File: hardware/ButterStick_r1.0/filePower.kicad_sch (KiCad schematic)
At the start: 65 parts, among them J7 Conn_01x02_Male, Q4 Q_PMOS_GSD, Q5 Q_NMOS_GSD, U10 TLV62569DRL, U16 TLV75801PDRV, U17 TLV75801PDRV, U18 TLV6001DCK, U19 LM74700, U6 TLV62569DRL, U7 TLV62569DRL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

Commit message: hw.r1d0: Review complete, gerbers generated
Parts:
- removed Q4: Q_PMOS_GSD, Package_TO_SOT_SMD:SOT-23, symbol Device:Q_PMOS_GSD
- removed Q5: Q_NMOS_GSD, Package_TO_SOT_SMD:SOT-23, symbol Device:Q_NMOS_GSD
- removed U18: TLV6001DCK, Package_TO_SOT_SMD:SOT-353_SC-70-5, symbol Amplifier_Operational:TLV6001DCK
- added C165: 150uF, Capacitor_SMD:CP_Elec_5x4.4, symbol Device:CP1
- added C166: 1uF, Capacitor_SMD:C_0402_1005Metric, symbol Device:C
- added C167: 0.1uF, Capacitor_SMD:C_0402_1005Metric, symbol Device:C
- added Q4: Q_NMOS_GSD, Package_SON:Diodes_PowerDI3333-8, symbol Device:Q_NMOS_GSD
- added R95: 23.7k, Resistor_SMD:R_0402_1005Metric, symbol Device:R
- added U18: TPS2121, gkl_housings_qfn:VQFN-HR, symbol gkl_pmic:TPS2121
- C144: value 0.1uF -> 0.01uF; SN-DK 1276-1002-1-ND -> (none)
- C29, C61, C76, C77, C78: value 0.1uF -> 4.7uF
- C31: value 1uF -> 4.7uF
- C55, C74, C82, C83, C84: value 4.7uF -> 10uF
- C75, C85, C86, C87: value 0.1uF -> 1uF
- R60, R73, R74, R90: value 13.0K -> 180k
- R91: value 53.6K -> 23.7k
- R92, R96: value 53.6K -> 5k
- R97: value 53.6K -> 47k; Tol 1% -> (none)
- U16, U17: PN (none) -> TLV75801PDRVR
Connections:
- net +5V: now also C165.1, U18.1 (OUT), U18.8 (OUT); no longer R96.2, U19.4 (CATHODE)
- net GND: now also C144.2, R96.1, C165.2, C166.2, U18.12 (GND), U18.3 (CP2), U18.6 (PR1), U18.9 (ST)
- net VBUS_USB: now also R91.2, U18.7 (IN1)
- net at J7.1 (Pin_1), U19.3 (EN), U19.6 (ANODE): now also C166.1, C167.1, Q4.3 (D); no longer C143.1, C144.1, R91.2
- net at R91.1, R92.2: now also U18.5 (OV1)
- net at R97.2: now also U18.10 (ILIM); no longer R96.1
- net at U19.5 (GATE): now also Q4.1 (G)
- net at U19.1 (VCAP): now also C167.2; no longer C144.2
- net P_1V2_A renamed P_1V1_A
- net P_1V2_T renamed P_1V1_T
- new net: C143.1, Q4.2 (S), R95.2, U18.2 (IN2), U19.4 (CATHODE)
- new net: R95.1, R96.2, U18.4 (OV2)
- new net: C144.1, U18.11 (SS)
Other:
- note added: "IN2 takes priority over IN1"
- moved on the sheet: C143, C29, C31, C41, C54, C55, C57, C61, C68, C73, C74, C75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

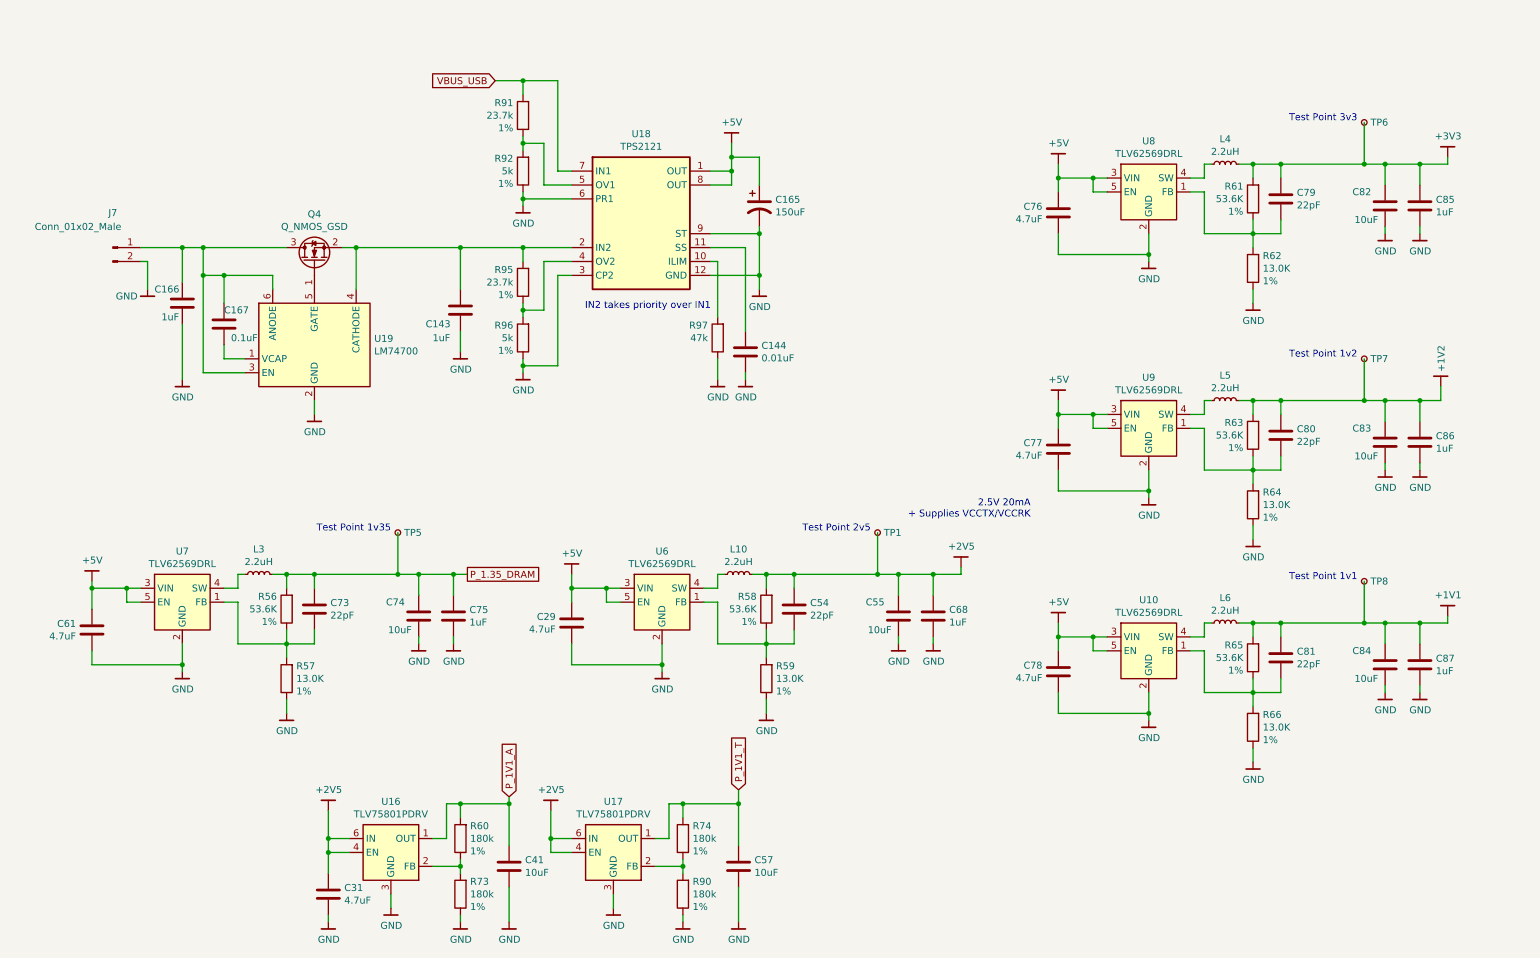
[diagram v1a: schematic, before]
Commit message: hw.r1d0: Update BOM fieids in schematic.
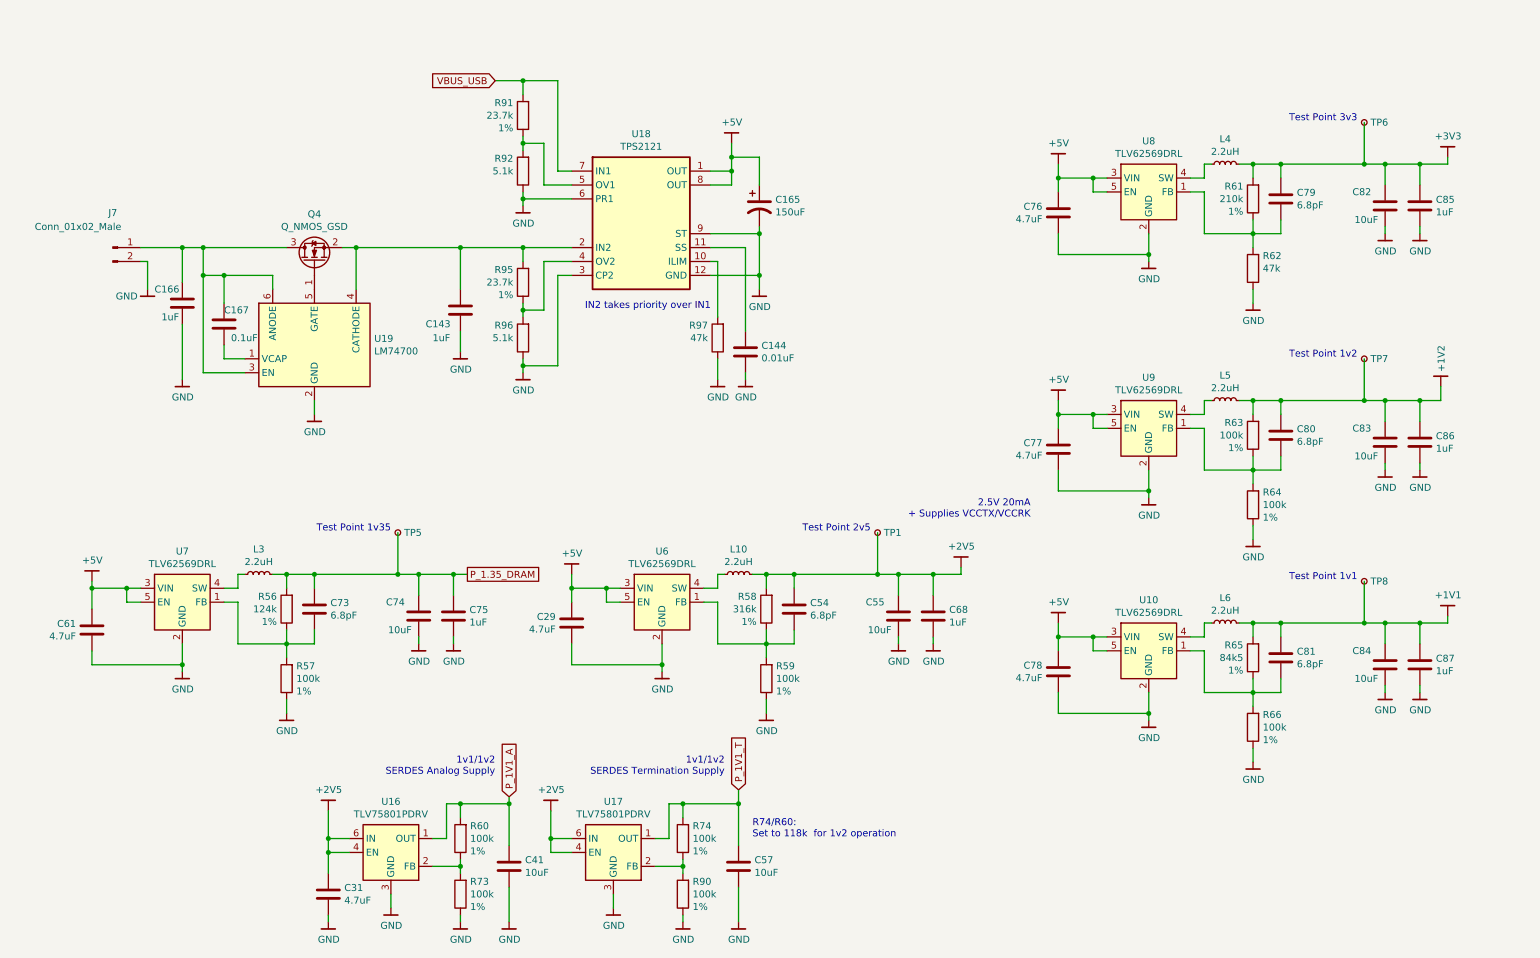
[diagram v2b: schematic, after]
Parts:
- C143, C166: Mfg Samsung Electro-Mechanics -> Yageo; PN CL05B104KP5NNNC -> CC0402KRX5R6BB105; SN-DK 1276-1002-1-ND -> (none)
- C144: Mfg Samsung Electro-Mechanics -> Yageo
- C165: Mfg (none) -> United Chemi-Con
- C167: Mfg Samsung Electro-Mechanics -> Yageo; PN CL05B104KP5NNNC -> CC0402KRX5R6BB104; SN-DK 1276-1002-1-ND -> (none); Tol (none) -> 10V / X5R
- C29, C61, C76, C77, C78: Mfg Samsung Electro-Mechanics -> Yageo; PN CL05B104KP5NNNC -> CC0402MRX5R6BB475
- C31: Mfg Samsung Electro-Mechanics -> Yageo; PN CL05A105KP5NNNC -> CC0402MRX5R6BB475; SN-DK 445-13185-1-ND -> (none)
- C41, C57: Mfg (none) -> Yageo; PN CL10A106MP8NNNC -> CC0603KRX5R5BB106; SN-DK 445-7486-1-ND -> (none)
- C54, C73, C79, C80, C81: value 22pF -> 6.8pF; Mfg Samsung Electro-Mechanics -> Yageo; PN CL05B104KP5NNNC -> CC0402CRNPO9BN6R8
- C55, C74, C82, C83, C84: Mfg Samsung Electro-Mechanics -> Yageo; PN CL10A475KP8NNNC -> CC0603KRX5R5BB106
- C68: Mfg Samsung Electro-Mechanics -> Yageo; PN CL05A105KP5NNNC -> CC0402KRX5R6BB105; SN-DK 445-13185-1-ND -> (none)
- C75, C85, C86, C87: Mfg Samsung Electro-Mechanics -> Yageo; PN CL05B104KP5NNNC -> CC0402KRX5R6BB105
- J7, TP1, TP5, TP6, TP7, TP8: PN (none) -> DNP
- L10, L3, L4, L5, L6: Mfg (none) -> Sunltech Tech; PN (none) -> SLM20122R2MIT
- Q4: Mfg (none) -> Diodes Incorporated
- R56: value 53.6K -> 124k; Mfg Stackpole Electronics Inc -> Yageo; PN (none) -> RC0402FR-07124KL
- R57, R59, R64, R66: value 13.0K -> 100k; Mfg Stackpole Electronics Inc -> Yageo; PN (none) -> RC0402FR-07100KL
- R58: value 53.6K -> 316k; Mfg Stackpole Electronics Inc -> Yageo; PN (none) -> RC0402FR-07316KL
- R60, R73, R74, R90: value 180k -> 100k; Mfg Stackpole Electronics Inc -> Yageo; PN (none) -> RC0402FR-07100KL
- R61: value 53.6K -> 210k; Mfg Stackpole Electronics Inc -> Yageo; PN (none) -> RC0402FR-07210KL
- R62: value 13.0K -> 47k; Mfg Stackpole Electronics Inc -> Yageo; PN (none) -> RC0402FR-074KL; Tol 1% -> (none)
- R63: value 53.6K -> 100k; Mfg Stackpole Electronics Inc -> Yageo; PN (none) -> RC0402FR-07100KL
- R65: value 53.6K -> 84k5; Mfg Stackpole Electronics Inc -> Yageo; PN (none) -> RC0402FR-0784K5L
- R91, R95: Mfg Stackpole Electronics Inc -> Yageo; PN (none) -> RC0402FR-0723K7L
- R92, R96: value 5k -> 5.1k; Mfg Stackpole Electronics Inc -> Yageo; PN (none) -> RC0402FR-075K1L; Tol 1% -> (none)
- R97: Mfg Stackpole Electronics Inc -> Yageo; PN (none) -> RC0402FR-074KL
- U10, U6, U7, U8, U9: Mfg (none) -> Texas Instruments; PN (none) -> TLV62569DRLR
- U16, U17: Mfg (none) -> Texas Instruments
- U18: Mfg (none) -> Texas Instruments; PN (none) -> TPS2121RUXR
- U19: Mfg (none) -> Texas Instruments; PN (none) -> LM74700QDBVRQ1
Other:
- note added: "1v1/1v2 SERDES Analog Supply"
- note added: "1v1/1v2 SERDES Termination Supply"
- note added: "R74/R60: Set to 118k for 1v2 operation"

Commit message: hw.r1d0: Fix RGMII straps
This commit correctly sets the stop resistos on the RGMII lines to 1K5
instead of DNP.
Also regenerate and add a schematic in PDF format.

Fixes #6
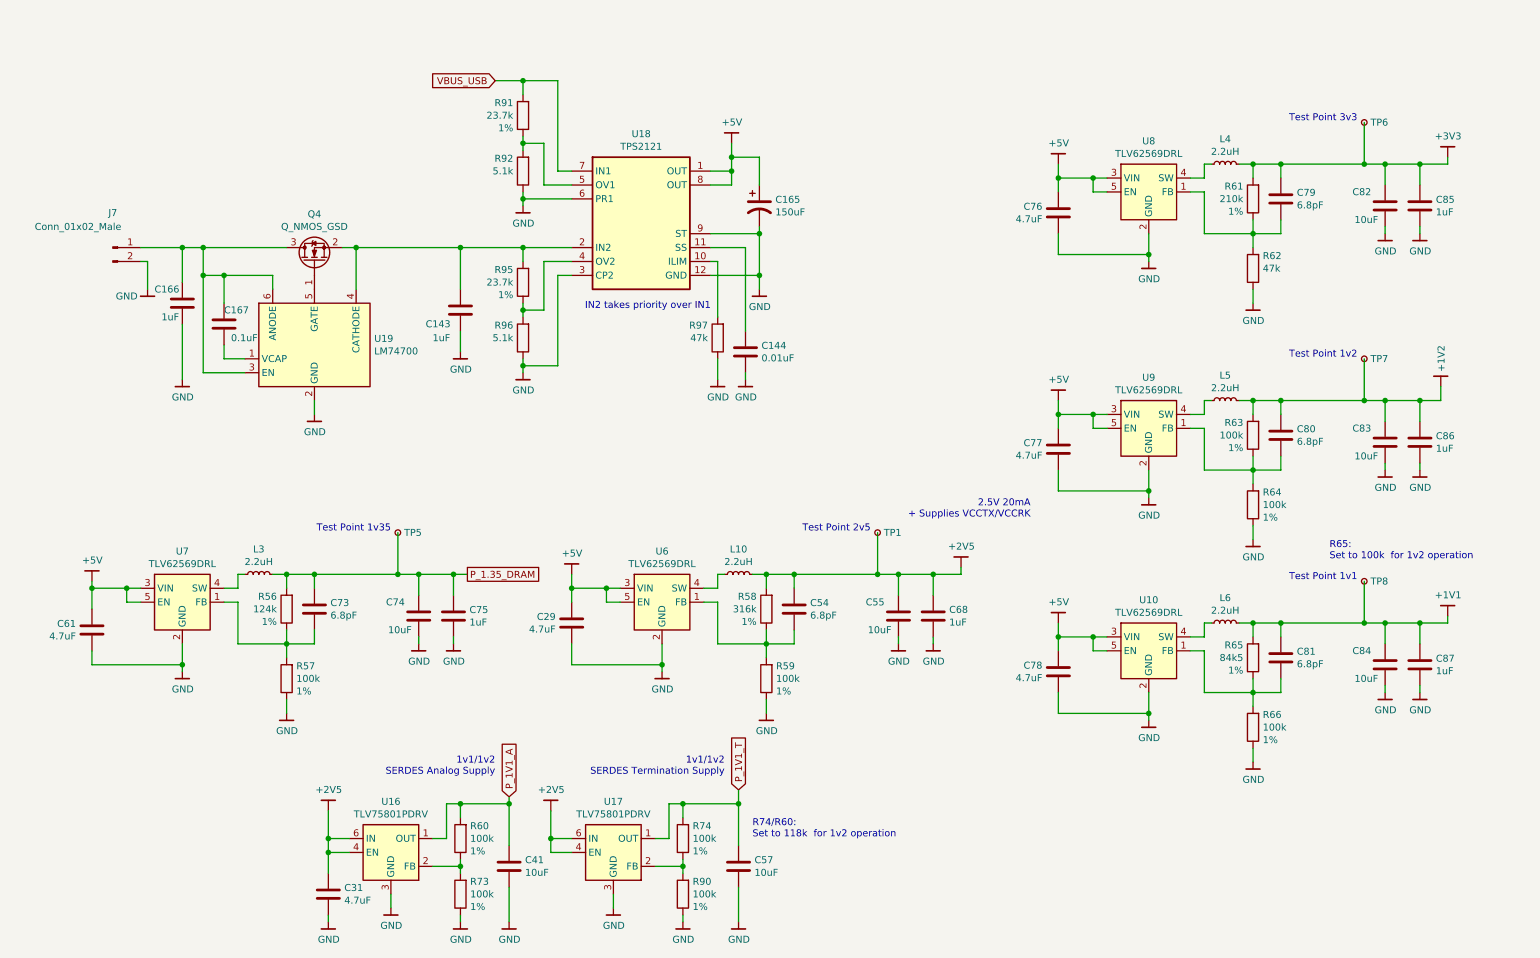
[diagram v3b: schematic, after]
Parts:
- C144: PN CL05B104KP5NNNC -> CC0402KRX7R8BB103
- C29, C31, C61, C76, C77, C78: PN CC0402MRX5R6BB475 -> CC0402KRX5R6BB475
- R62, R97: PN RC0402FR-074KL -> RC0402FR-0747KL
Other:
- note added: "R65: Set to 100k for 1v2 operation"

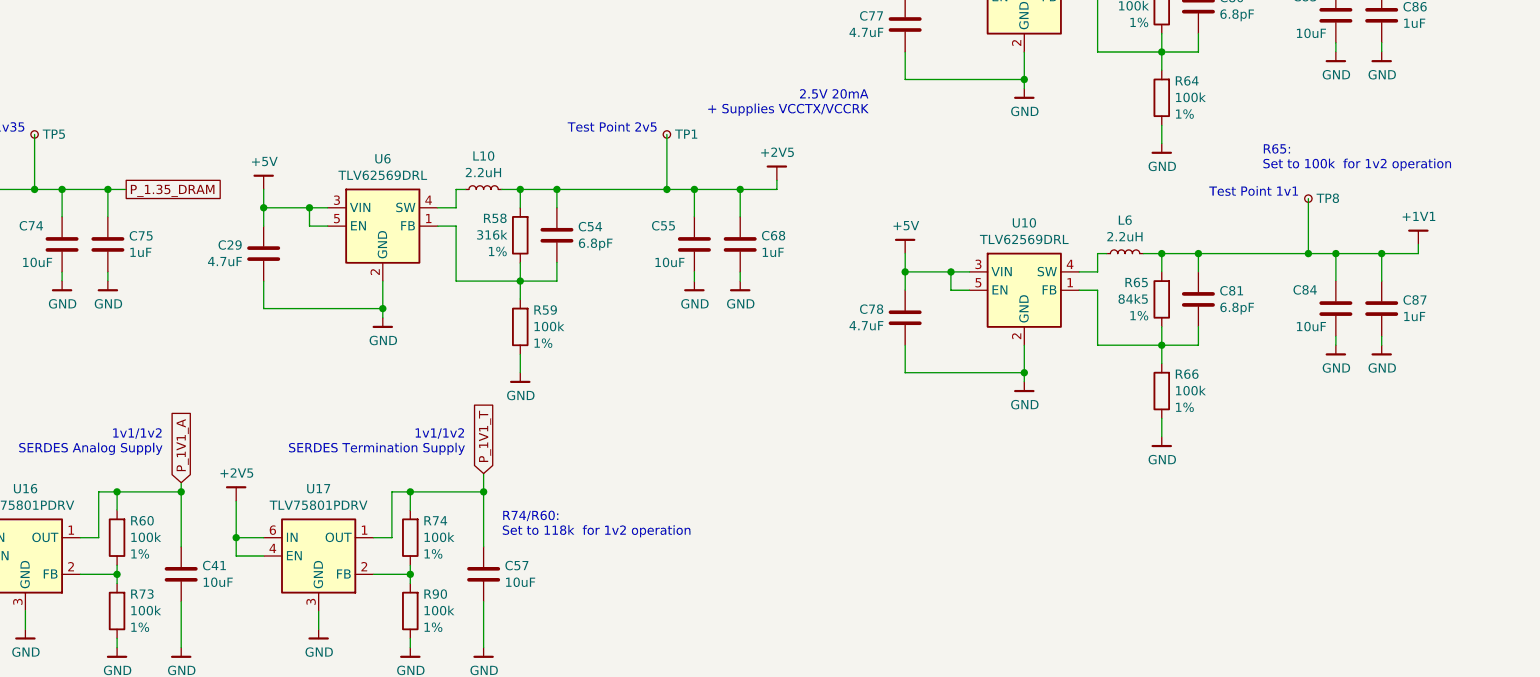
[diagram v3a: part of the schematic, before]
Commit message: hardware.r1d0: Update BOM values in schematic
Regenerate schematics and export BOM

Fixes #9
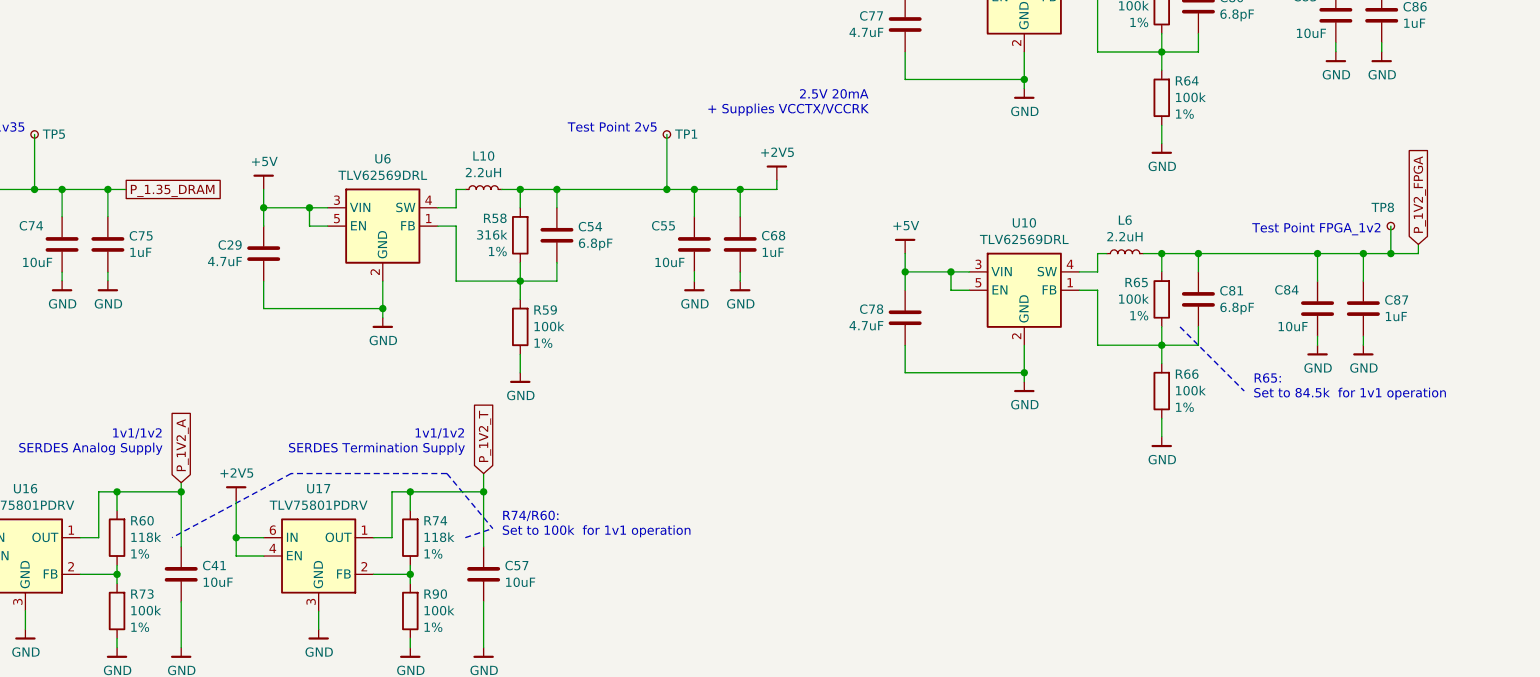
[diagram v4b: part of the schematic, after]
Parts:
- R60, R74: value 100k -> 118k; PN RC0402FR-07100KL -> RC0402FR-07118KL
- R65: value 84k5 -> 100k; PN RC0402FR-0784K5L -> RC0402FR-07100KL
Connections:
- net +1V1 renamed P_1V2_FPGA
- net P_1V1_A renamed P_1V2_A
- net P_1V1_T renamed P_1V2_T
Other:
- note added: "R65: Set to 84.5k for 1v1 operation"
- note added: "R74/R60: Set to 100k for 1v1 operation"
- note added: "Test Point FPGA_1v2"
- note removed: "R65: Set to 100k for 1v2 operation"
- note removed: "R74/R60: Set to 118k for 1v2 operation"
- note removed: "Test Point 1v1"
- moved on the sheet: C84, C87, TP8

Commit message: hardware.r1d0: Tidy up BOM entries
Export HTML Interactive BOM
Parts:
- J7: now left out of the parts list
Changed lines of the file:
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@@
   )
   (symbol (lib_id "Connector:Conn_01x02_Male") (at 27.94 62.23 0) (unit 1)
-    (in_bom yes) (on_board yes)
+    (in_bom no) (on_board yes)
     (property "Reference" "J7" (id 0) (at 27.94 55.88 0))
     (property "Value" "Conn_01x02_Male" (id 1) (at 21.59 58.42 0))
